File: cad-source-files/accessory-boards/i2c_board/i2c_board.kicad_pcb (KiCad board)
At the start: 2 copper layers, 50 x 22 mm, 7 parts, among them J2 Conn_01x03, J5 Conn_01x03, J7 Conn_01x03, J8 Conn_01x03, J9 Conn_01x06_MountingPin

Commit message: qwiic quick board
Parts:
- removed J2, J5, J7, J8: Conn_01x03, Connector_JST:JST_PH_B3B-PH-SM4-TB_1x03-1MP_P2.00mm_Vertical
- added D1: led_g, LED_SMD:LED_0603_1608Metric, F.Cu at (165.8, 76.7)
- added J1: Conn_01x04_MountingPin, Connector_JST:JST_SH_SM04B-SRSS-TB_1x04-1MP_P1.00mm_Horizontal, F.Cu at (188.8, 76.7)
- added JP1: Jumper_2_Open, Jumper:SolderJumper-2_P1.3mm_Bridged_RoundedPad1.0x1.5mm, B.Cu at (176.0, 81.5)
- added JP2: Jumper_2_Open, Jumper:SolderJumper-2_P1.3mm_Bridged_RoundedPad1.0x1.5mm, B.Cu at (182.8, 81.5)
- added R1: 10k, Resistor_SMD:R_0603_1608Metric, F.Cu at (168.0, 85.5)
- added R2: 4.7k, Resistor_SMD:R_0603_1608Metric, F.Cu at (171.0, 85.5)
- added R3: 4.7k, Resistor_SMD:R_0603_1608Metric, F.Cu at (174.0, 85.5)
- added R4: 10k, Resistor_SMD:R_0603_1608Metric, F.Cu at (165.0, 85.5)
- added SW1: SW_Push, Button_Switch_SMD:SWITCH_2x3_SMD_TACTILE_GREEN, F.Cu at (175.0, 76.7)
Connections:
- J9 pad 1: /A -> /D
- J9 pad 2: /B -> /C
- J9 pad 3: /C -> /B
- J9 pad 4: /D -> /A
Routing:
- net /D: track 8.98 -> 48.0 mm, vias 0 -> 1
- net /C: track 18.7 -> 43.1 mm, vias 0 -> 1
- net /A: track 41.0 -> 17.2 mm
- net Net-(JP2-Pad2): track 0.00 -> 12.9 mm, vias 0 -> 1
- net +3V3: track 37.1 -> 45.9 mm
- net Net-(D1-Pad2): track 0.00 -> 7.98 mm
- net Net-(JP1-Pad2): track 0.00 -> 6.63 mm, vias 0 -> 1
- net /B: track 28.2 -> 29.6 mm
- net GND: vias 32 -> 69
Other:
- board text added: "C SCL"
- board text added: "D SDA"
- board text added: "I2C Expansion Board"
- board text added: "cut to remove pullup resistors"
- board text removed: "+"
- board text removed: "Ports"
- board text removed: "S"

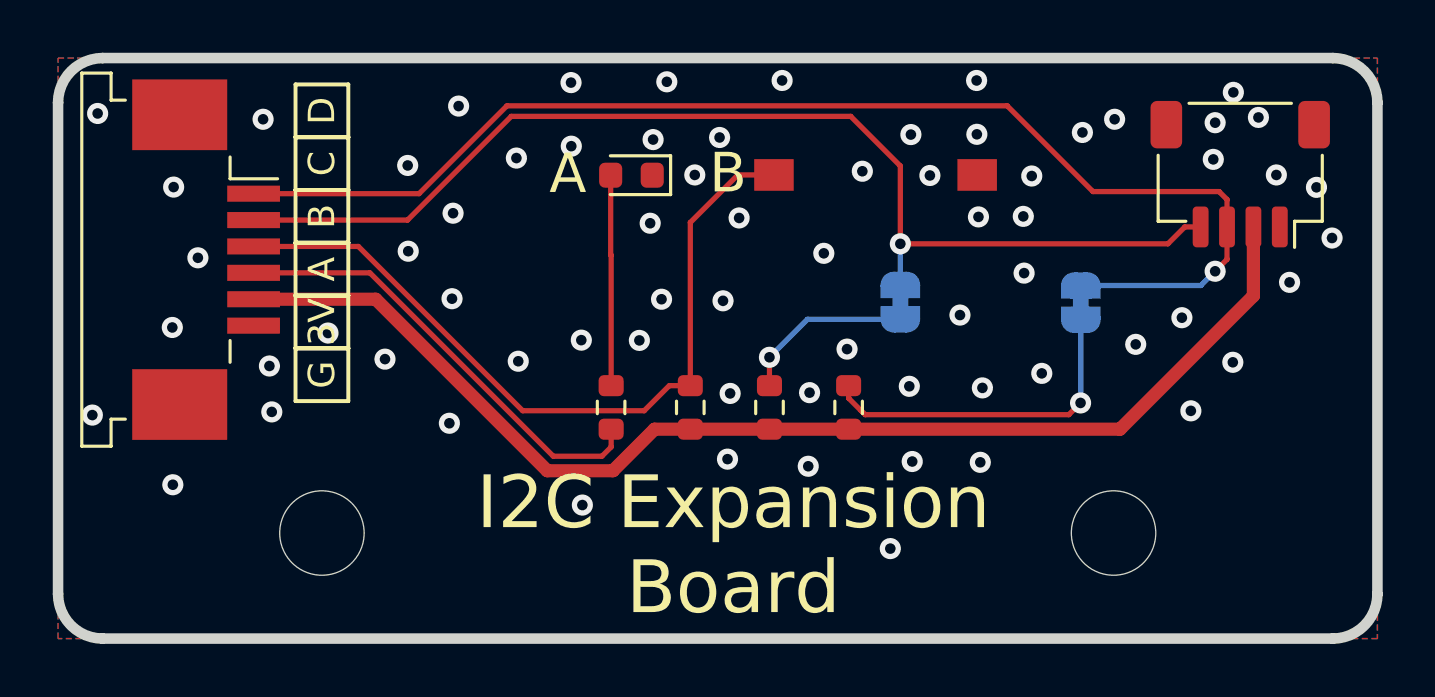
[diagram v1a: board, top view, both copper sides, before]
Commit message: mo 4 has spawned
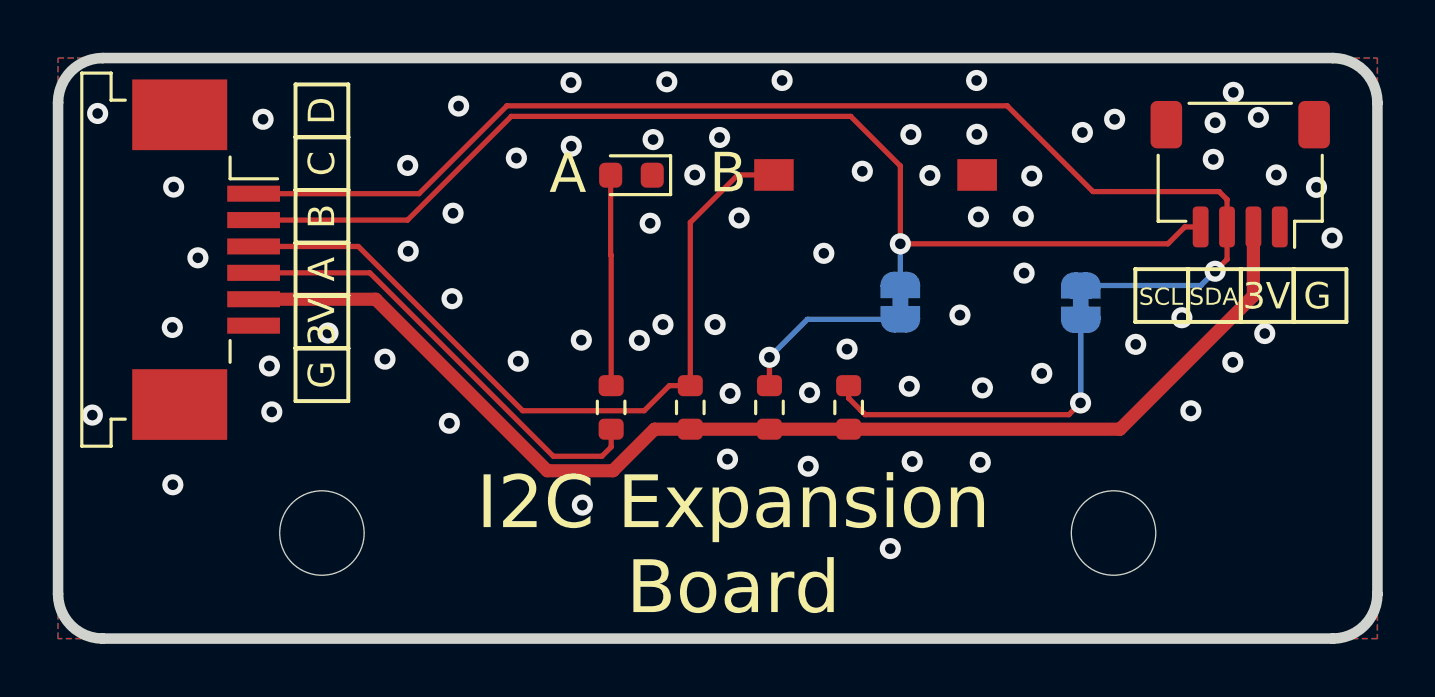
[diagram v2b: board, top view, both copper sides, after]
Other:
- board text added: "SCL"
- board text added: "SDA"
- board text added: "qwiic & stemma compatible"
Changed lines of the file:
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@@
   (gr_rect (start 155.05 81.25) (end 153.05 79.25) (layer "F.SilkS") (width 0.15) (fill none))
   (gr_rect (start 155.05 77.25) (end 153.05 75.25) (layer "F.SilkS") (width 0.15) (fill none))
+  (gr_rect (start 186.875 82.25) (end 188.875 80.25) (layer "F.SilkS") (width 0.15) (fill none))
+  (gr_rect (start 190.875 82.25) (end 192.875 80.25) (layer "F.SilkS") (width 0.15) (fill none))
+  (gr_rect (start 184.875 82.25) (end 186.875 80.25) (layer "F.SilkS") (width 0.15) (fill none))
   (gr_rect (start 155.05 79.25) (end 153.05 77.25) (layer "F.SilkS") (width 0.15) (fill none))
+  (gr_rect (start 188.875 82.25) (end 190.875 80.25) (layer "F.SilkS") (width 0.15) (fill none))
   (gr_rect (start 155.05 75.25) (end 153.05 73.25) (layer "F.SilkS") (width 0.15) (fill none))
   (gr_rect (start 155.05 85.25) (end 153.05 83.25) (layer "F.SilkS") (width 0.15) (fill none))
@@
     (effects (font (size 1.3 1.3) (thickness 0.3)) (justify mirror))
   )
+  (gr_text "qwiic & stemma\ncompatible" (at 167.125 80.575) (layer "B.SilkS")
+    (effects (font (size 0.7 0.7) (thickness 0.175)) (justify mirror))
+  )
   (gr_text "D\nSDA" (at 182.8 85.14) (layer "B.SilkS")
     (effects (font (size 1.2 1.2) (thickness 0.3)) (justify mirror))
@@
     (effects (font (size 1 1) (thickness 0.15)))
   )
+  (gr_text "3V" (at 189.85 81.275) (layer "F.SilkS")
+    (effects (font (size 1 1) (thickness 0.15)))
+  )
   (gr_text "B" (at 169.44 76.61) (layer "F.SilkS")
     (effects (font (size 1.5 1.5) (thickness 0.375)))
   )
+  (gr_text "SDA" (at 187.85 81.3) (layer "F.SilkS")
+    (effects (font (size 0.65 0.65) (thickness 0.15)))
+  )
+  (gr_text "G" (at 191.775 81.275) (layer "F.SilkS")
+    (effects (font (size 1 1) (thickness 0.15)))
+  )
   (gr_text "I2C Expansion \nBoard" (at 169.64 90.71) (layer "F.SilkS")
     (effects (font (size 2 2) (thickness 0.5)))
@@
   (gr_text "G" (at 154.05 84.25 90) (layer "F.SilkS")
     (effects (font (size 1 1) (thickness 0.15)))
+  )
+  (gr_text "SCL" (at 185.85 81.3) (layer "F.SilkS")
+    (effects (font (size 0.65 0.65) (thickness 0.15)))
   )
   (gr_text "C" (at 154.05 76.25 90) (layer "F.SilkS")
@@
   (via (at 187.9 74.7) (size 0.8) (drill 0.4) (layers "F.Cu" "B.Cu") (free) (net 1))
   (via (at 169.12 75.26) (size 0.8) (drill 0.4) (layers "F.Cu" "B.Cu") (free) (net 1))
-  (via (at 169.25 81.45) (size 0.8) (drill 0.4) (layers "F.Cu" "B.Cu") (free) (net 1))
+  (via (at 168.95 82.35) (size 0.8) (drill 0.4) (layers "F.Cu" "B.Cu") (free) (net 1))
   (via (at 178.23 81.99) (size 0.8) (drill 0.4) (layers "F.Cu" "B.Cu") (free) (net 1))
   (via (at 149.35 79.82) (size 0.8) (drill 0.4) (layers "F.Cu" "B.Cu") (free) (net 1))
@@
   (via (at 166.6 75.34) (size 0.8) (drill 0.4) (layers "F.Cu" "B.Cu") (free) (net 1))
   (via (at 156.44 83.66) (size 0.8) (drill 0.4) (layers "F.Cu" "B.Cu") (free) (net 1))
-  (via (at 190.72 80.75) (size 0.8) (drill 0.4) (layers "F.Cu" "B.Cu") (free) (net 1))
+  (via (at 189.78 82.69) (size 0.8) (drill 0.4) (layers "F.Cu" "B.Cu") (free) (net 1))
   (via (at 180.95 76.72) (size 0.8) (drill 0.4) (layers "F.Cu" "B.Cu") (free) (net 1))
   (via (at 171.49 73.1) (size 0.8) (drill 0.4) (layers "F.Cu" "B.Cu") (free) (net 1))
@@
   (via (at 169.52 84.96) (size 0.8) (drill 0.4) (layers "F.Cu" "B.Cu") (free) (net 1))
   (via (at 148.43 77.14) (size 0.8) (drill 0.4) (layers "F.Cu" "B.Cu") (free) (net 1))
-  (via (at 166.92 81.39) (size 0.8) (drill 0.4) (layers "F.Cu" "B.Cu") (free) (net 1))
+  (via (at 166.975 82.35) (size 0.8) (drill 0.4) (layers "F.Cu" "B.Cu") (free) (net 1))
   (via (at 186.98 85.62) (size 0.8) (drill 0.4) (layers "F.Cu" "B.Cu") (free) (net 1))
   (via (at 169.86 78.31) (size 0.8) (drill 0.4) (layers "F.Cu" "B.Cu") (free) (net 1))
@@
     )
   )
+  (group "" (id c578c9b3-9bf9-4361-8fc4-e10b1171ff37)
+    (members
+      8b7222b9-ec62-4221-8377-ffabb4310ef8
+      a3714fab-c121-4c1b-8e54-e78e25a41883
+      ae4bf7fb-0e45-4ac6-a604-f45f26352d38
+      cbf1c397-888c-450d-bf40-02a7fe9a97a7
+    )
+  )

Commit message: 12-2 boards ordered
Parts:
- added G***: LOGO, Symbol:mustache_logo_16mm, B.Cu at (153.1, 77.2)
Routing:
- net GND: vias 69 -> 67
